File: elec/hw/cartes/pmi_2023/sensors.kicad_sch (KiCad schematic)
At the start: 51 parts, among them SW1 ESE22MH22, SW2 ESE22MH24, U10 tof_sensor_master, U12 LSM6DSO32XTR, U13 GP2S60B, U14 GP2S60B, U15 GP2S60B, U16 GP2S60B, U17 tof_sensor_master, U19 GP2S60B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

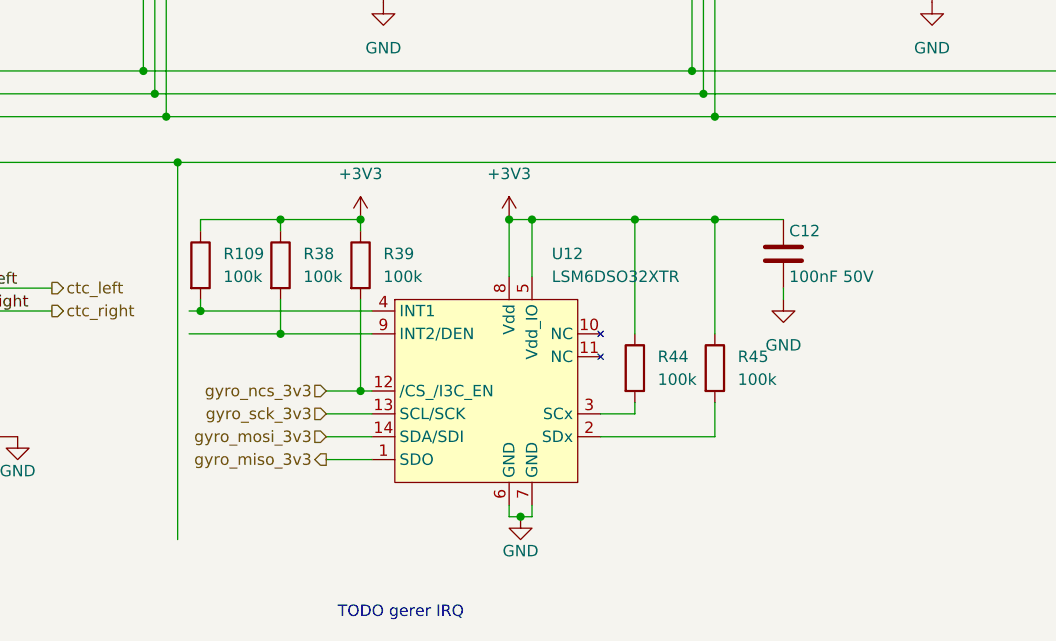
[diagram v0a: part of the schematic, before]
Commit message: pmi layout (WIP)
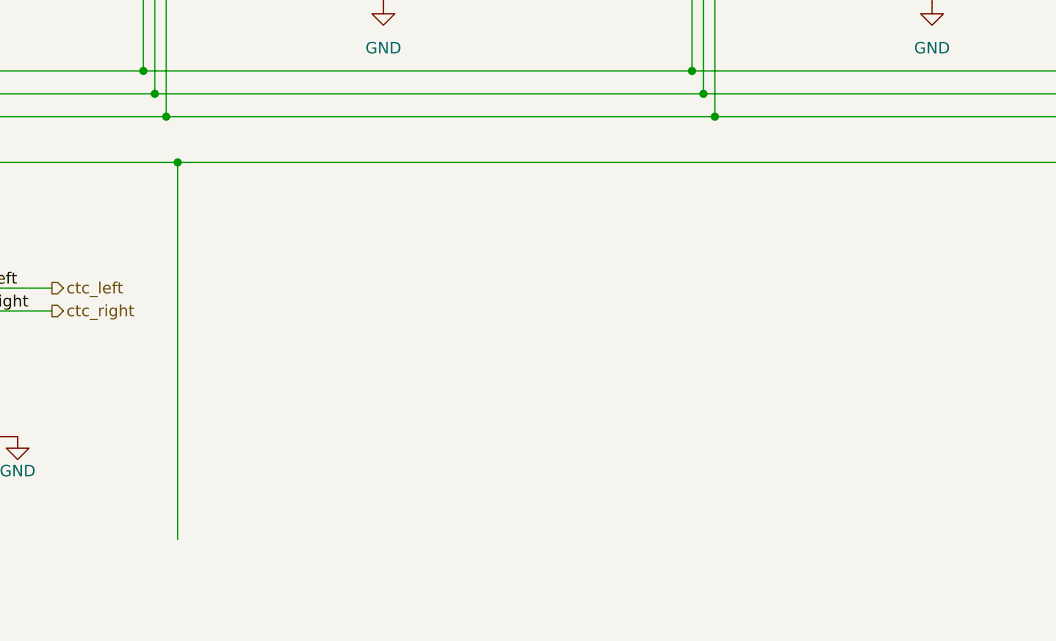
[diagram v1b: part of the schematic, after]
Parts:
- removed C12: 100nF 50V, cocotter_capacitors:C_0603_1608Metric, symbol cocotter_capacitors:C_100nF_50V_0603
- removed R109, R38, R39, R44, R45: 100k, cocotter_resistor:r0603_reflow, symbol cocotter_resistors:R_100k_0603_1%
- removed U12: LSM6DSO32XTR, cocotter_ic:LGA-14_3x2.5mm_P0.5mm_LayoutBorder3x4y, symbol cocotter_ic:LSM6DSO32XTR
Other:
- note removed: "TODO gerer IRQ"

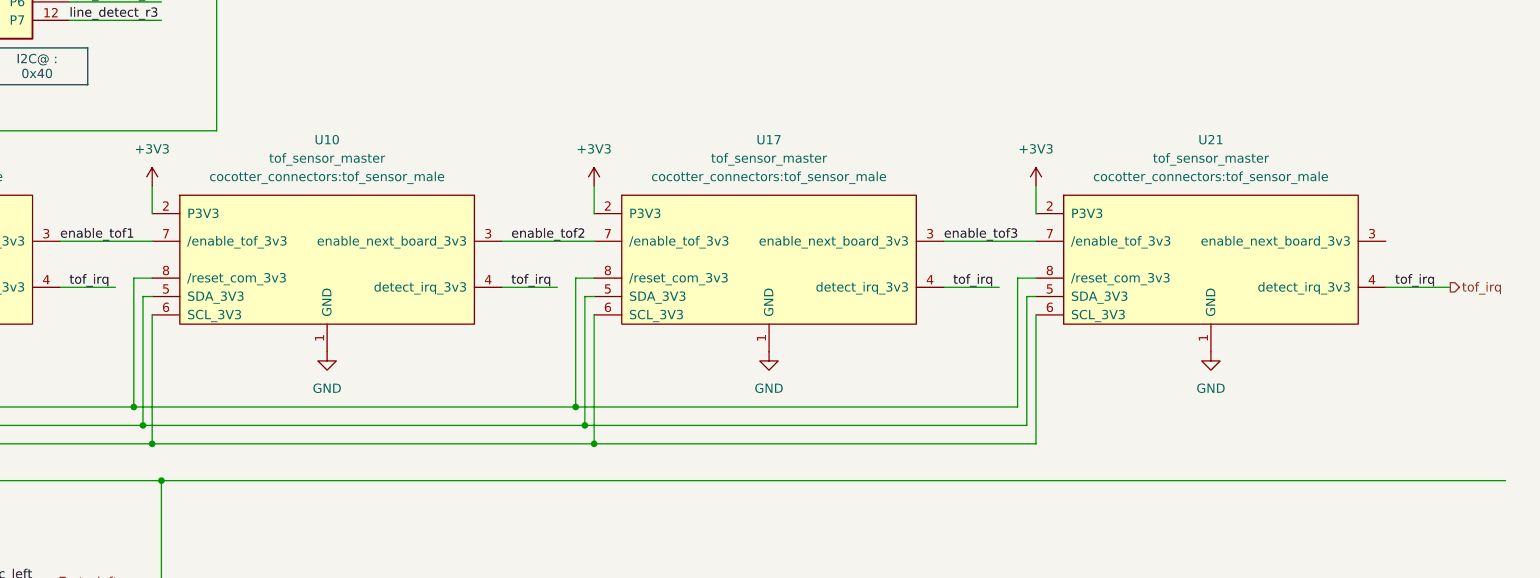
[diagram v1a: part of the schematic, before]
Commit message: front and back tof added, selector changed, ready to route
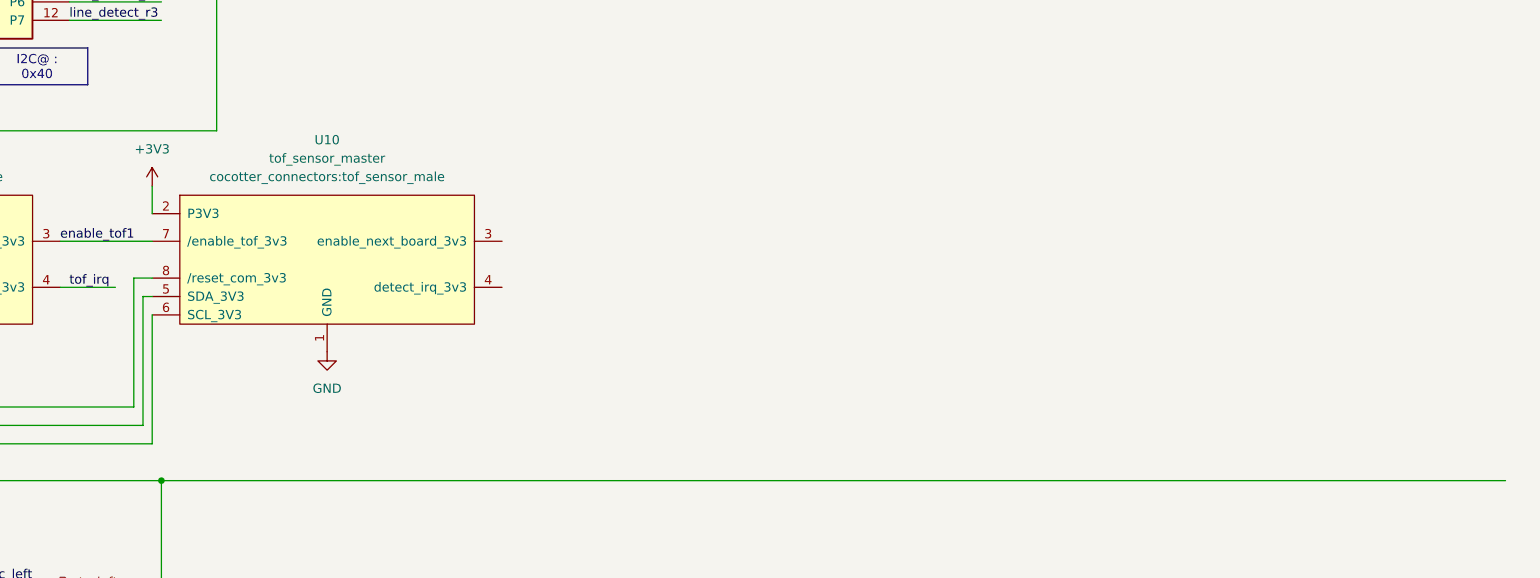
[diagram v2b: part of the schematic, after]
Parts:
- removed U17, U21: tof_sensor_master, cocotter_connectors:tof_sensor_male, symbol cocotter_connectors:tof_sensor_master
- R10, R11, R12: JLCPCB C21189 -> C431718
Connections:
- net tof_irq: no longer U10.4 (detect_irq_3v3)
- net enable_tof2: no longer names the net of U10.3 (enable_next_board_3v3)

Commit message: wip
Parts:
- R36, R37, R42, R43, R48, R49, R52, R53: mouser (none) -> 603-RC0603FR-10100KL
- U5: footprint cocotter_ic:SOT-23-5 -> cocotter_ic:SOT23-5
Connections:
- net ctc_rigth is gone; now on net ctc_right: R33.2, SW2.1
- net tof_irq: now also U10.4 (detect_irq_3v3)

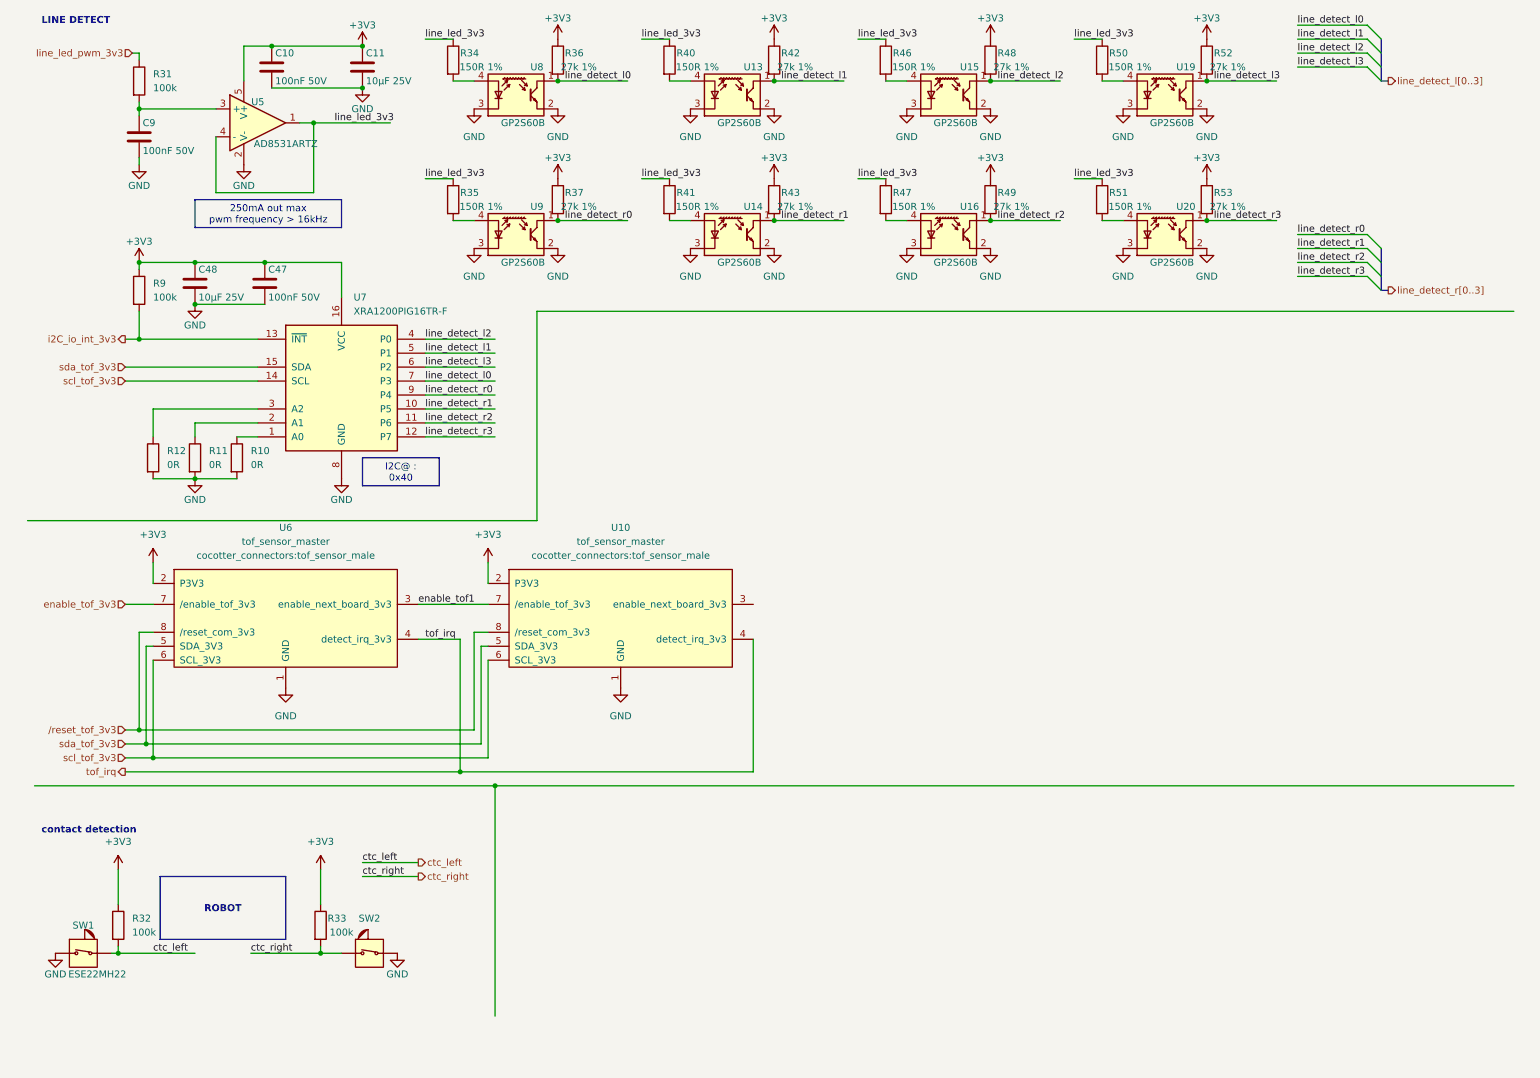
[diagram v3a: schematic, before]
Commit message: added oled display power supply res selectors, jlcpcb refs : wip
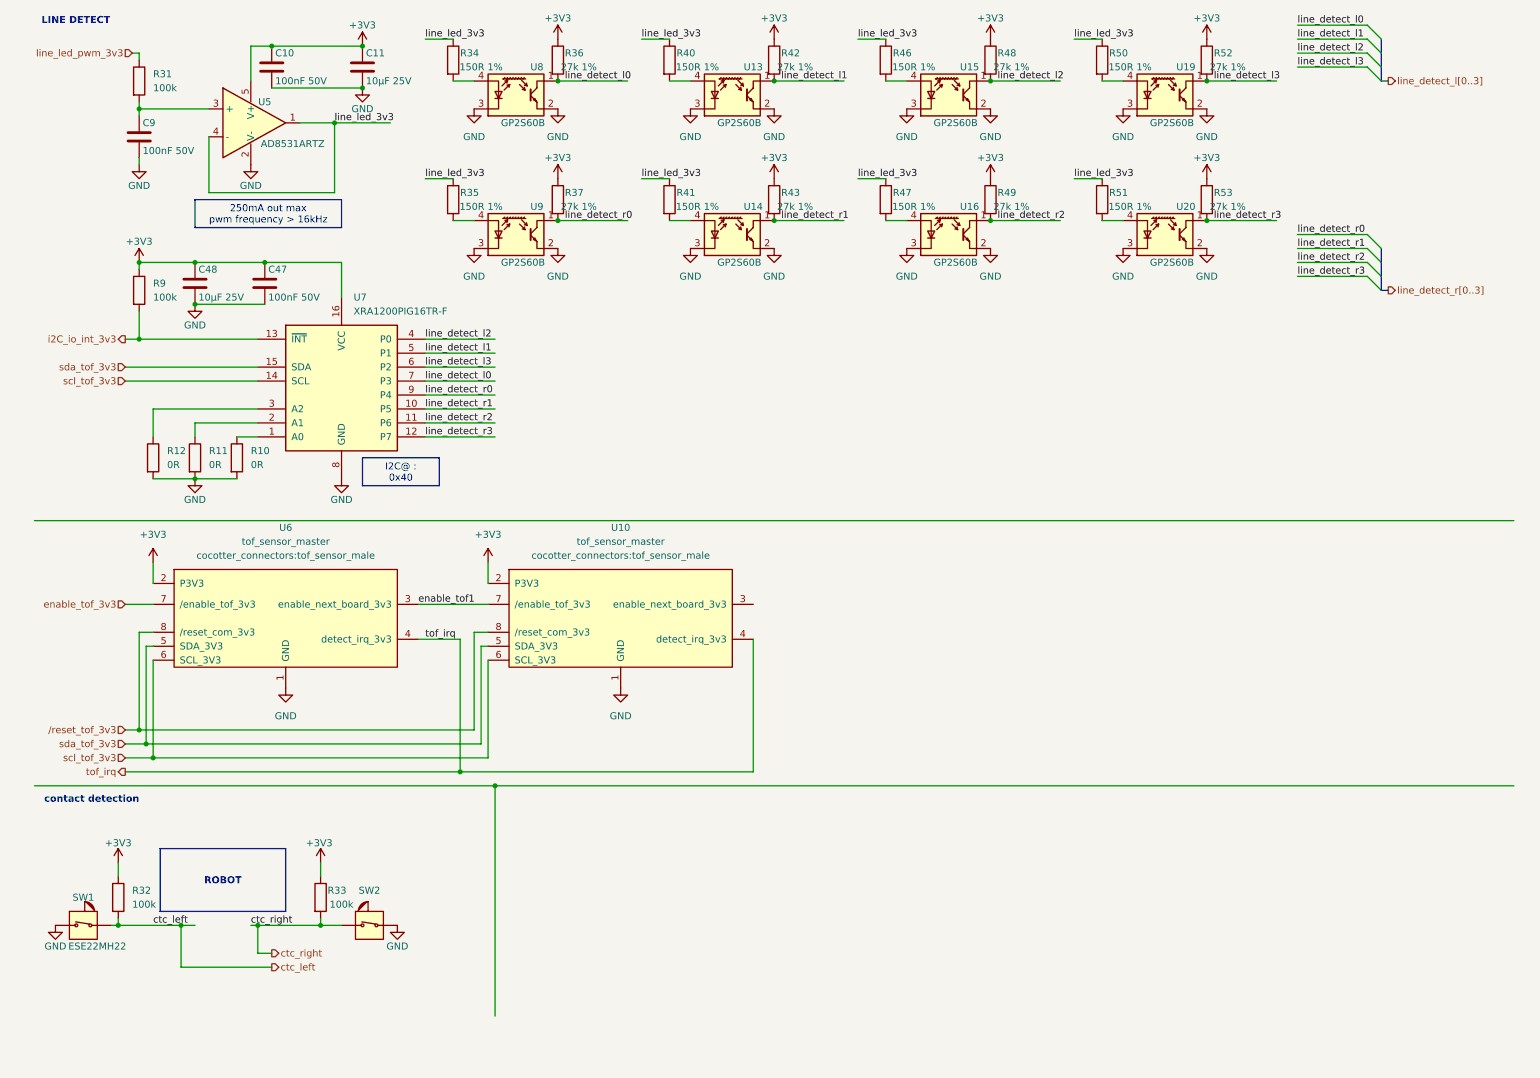
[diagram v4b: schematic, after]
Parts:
- C11, C48: symbol cocotter_capacitors:C_10µF_16V_0805_X5R -> cocotter_capacitors:C_10µF_25V_0805_X5R; Specification 10µF 25V X5R 0805 -> 10µF 25V X7R 0805
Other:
- moved on the sheet: R32, R33, SW1, SW2, U5

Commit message: reset button added to esp32 reset. uart prog connector replaces ftdi one
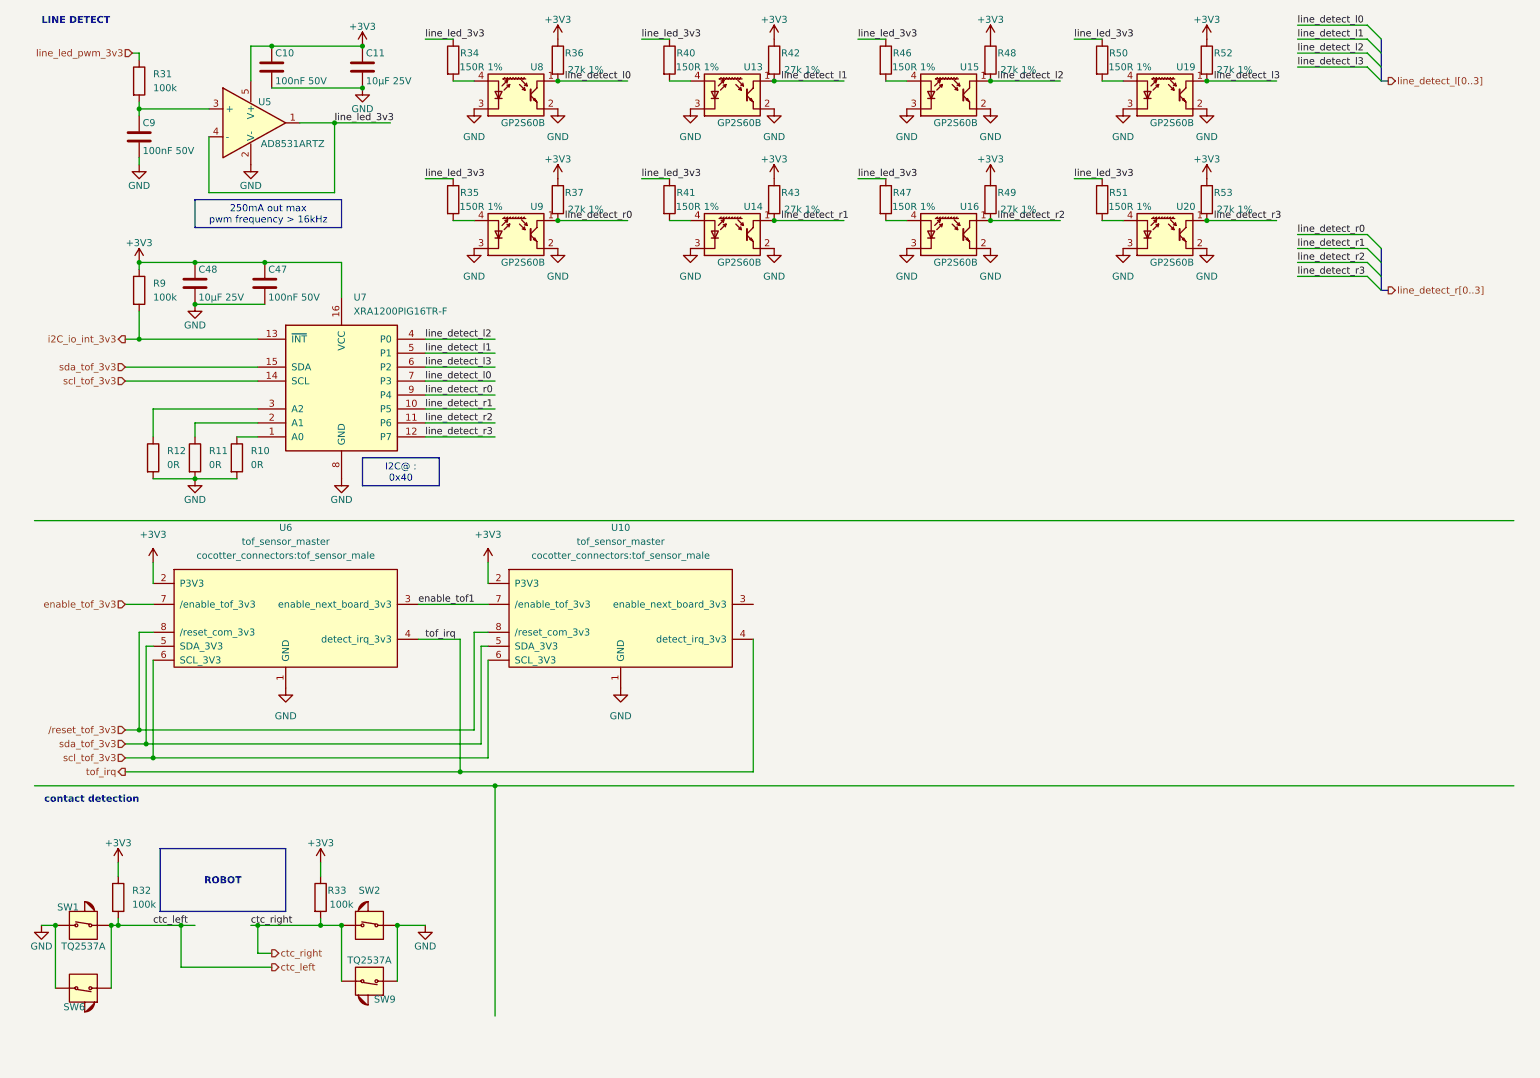
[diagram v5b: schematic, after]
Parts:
- removed SW1: ESE22MH22, cocotter_connectors:ESE22MH22, symbol cocotter_connectors:ESE22MH22
- added SW1, SW9: TQ2537A, cocotter_connectors:TQ2537A, symbol cocotter_connectors:TQ2537A
- added SW6: TQ2537, cocotter_connectors:TQ2537, symbol cocotter_connectors:TQ2537
- R34, R35, R36, R37, R40, R41, R42, R43, R46, R47, R48, R49, R50, R51, R52, R53: mouser 603-RC0603FR-10100KL -> (none)
- SW2: value ESE22MH24 -> TQ2537; footprint cocotter_connectors:ESE22MH24 -> cocotter_connectors:TQ2537; symbol cocotter_connectors:ESE22MH24 -> cocotter_connectors:TQ2537; Mouser 667-ESE-22MH24 -> C669818
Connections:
- net GND: now also SW1.1, SW6.2, SW9.1
- net ctc_left: now also SW1.2, SW6.1
- net ctc_right: now also SW9.2

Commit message: PAMI 2023: update jlc part number
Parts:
- SW1, SW9: JLCPCB (none) -> C669819
- SW2, SW6: JLCPCB (none) -> C669818
- U7: JLCPCB (none) -> C2669711
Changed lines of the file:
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@@
 			)
 		)
+		(property "JLCPCB" "C669819 "
+			(at 74.93 189.23 0)
+			(effects
+				(font
+					(size 1.27 1.27)
+				)
+				(hide yes)
+			)
+		)
 		(pin "2"
 		)
@@
 			)
 		)
+		(property "JLCPCB" "C669819 "
+			(at 22.86 179.07 0)
+			(effects
+				(font
+					(size 1.27 1.27)
+				)
+				(hide yes)
+			)
+		)
 		(pin "2"
 		)
@@
 			)
 		)
+		(property "JLCPCB" "C2669711"
+			(at 69.85 82.55 0)
+			(effects
+				(font
+					(size 1.27 1.27)
+				)
+				(hide yes)
+			)
+		)
 		(pin "2"
 		)
@@
 			)
 		)
+		(property "JLCPCB" "C669818"
+			(at 22.86 190.5 0)
+			(effects
+				(font
+					(size 1.27 1.27)
+				)
+				(hide yes)
+			)
+		)
 		(pin "2"
 		)
@@
 			(effects
 				(font
+					(size 1.27 1.27)
+				)
+				(hide yes)
+			)
+		)
+		(property "JLCPCB" "C669818"
+			(at 74.93 179.07 0)
+			(effects
+				(font
